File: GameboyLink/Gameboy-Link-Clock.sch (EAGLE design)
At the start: 37 parts, among them IC1 MEGA8-AI, J1 AVR_SPI_PRG_6PTH, Q1 16MHz, U1 DS1307Z, Y1 32.768kHz

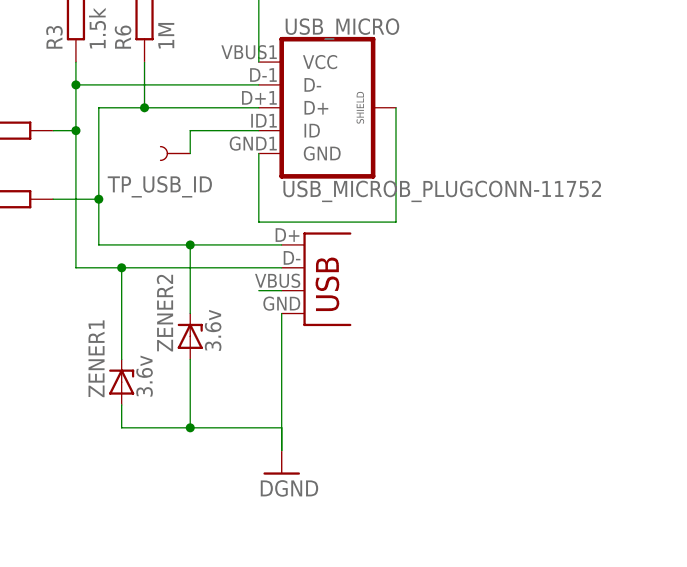
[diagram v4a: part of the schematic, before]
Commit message: Powers line done. Just noticed I forgot to wire ... THE GB LINK PORT to the MCU!!
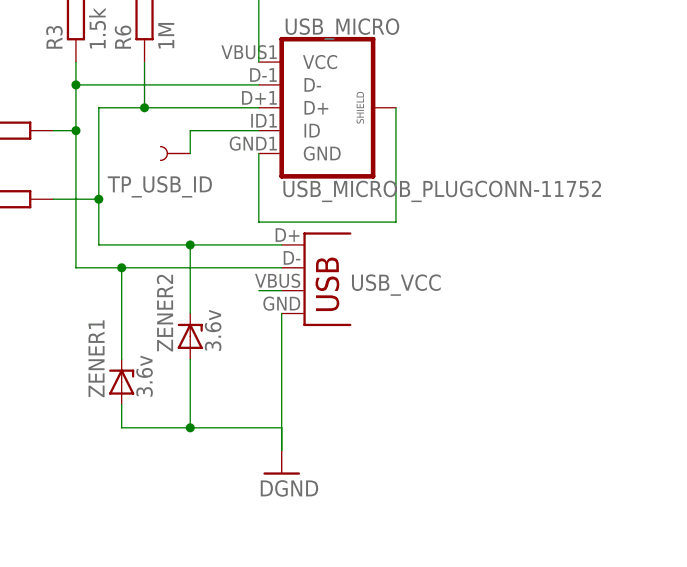
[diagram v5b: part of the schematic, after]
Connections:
- net USB_VCC: now also USB_MINI.VBUS
- net VCC: no longer USB_MINI.VBUS
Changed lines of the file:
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@@
-</segment>
-<segment>
-<pinref part="USB_MINI" gate="G$1" pin="VBUS"/>
-<wire x1="350.52" y1="-68.58" x2="353.06" y2="-68.58" width="0.1524" layer="91"/>
 </segment>
 <segment>
@@
 <label x="124.46" y="-45.72" size="1.778" layer="95"/>
 </segment>
-</net>
+<segment>
+<pinref part="USB_MINI" gate="G$1" pin="VBUS"/>
+<wire x1="350.52" y1="-68.58" x2="353.06" y2="-68.58" width="0.1524" layer="91"/>
+<label x="360.68" y="-68.58" size="1.778" layer="95"/>
+</segment>
+</net>

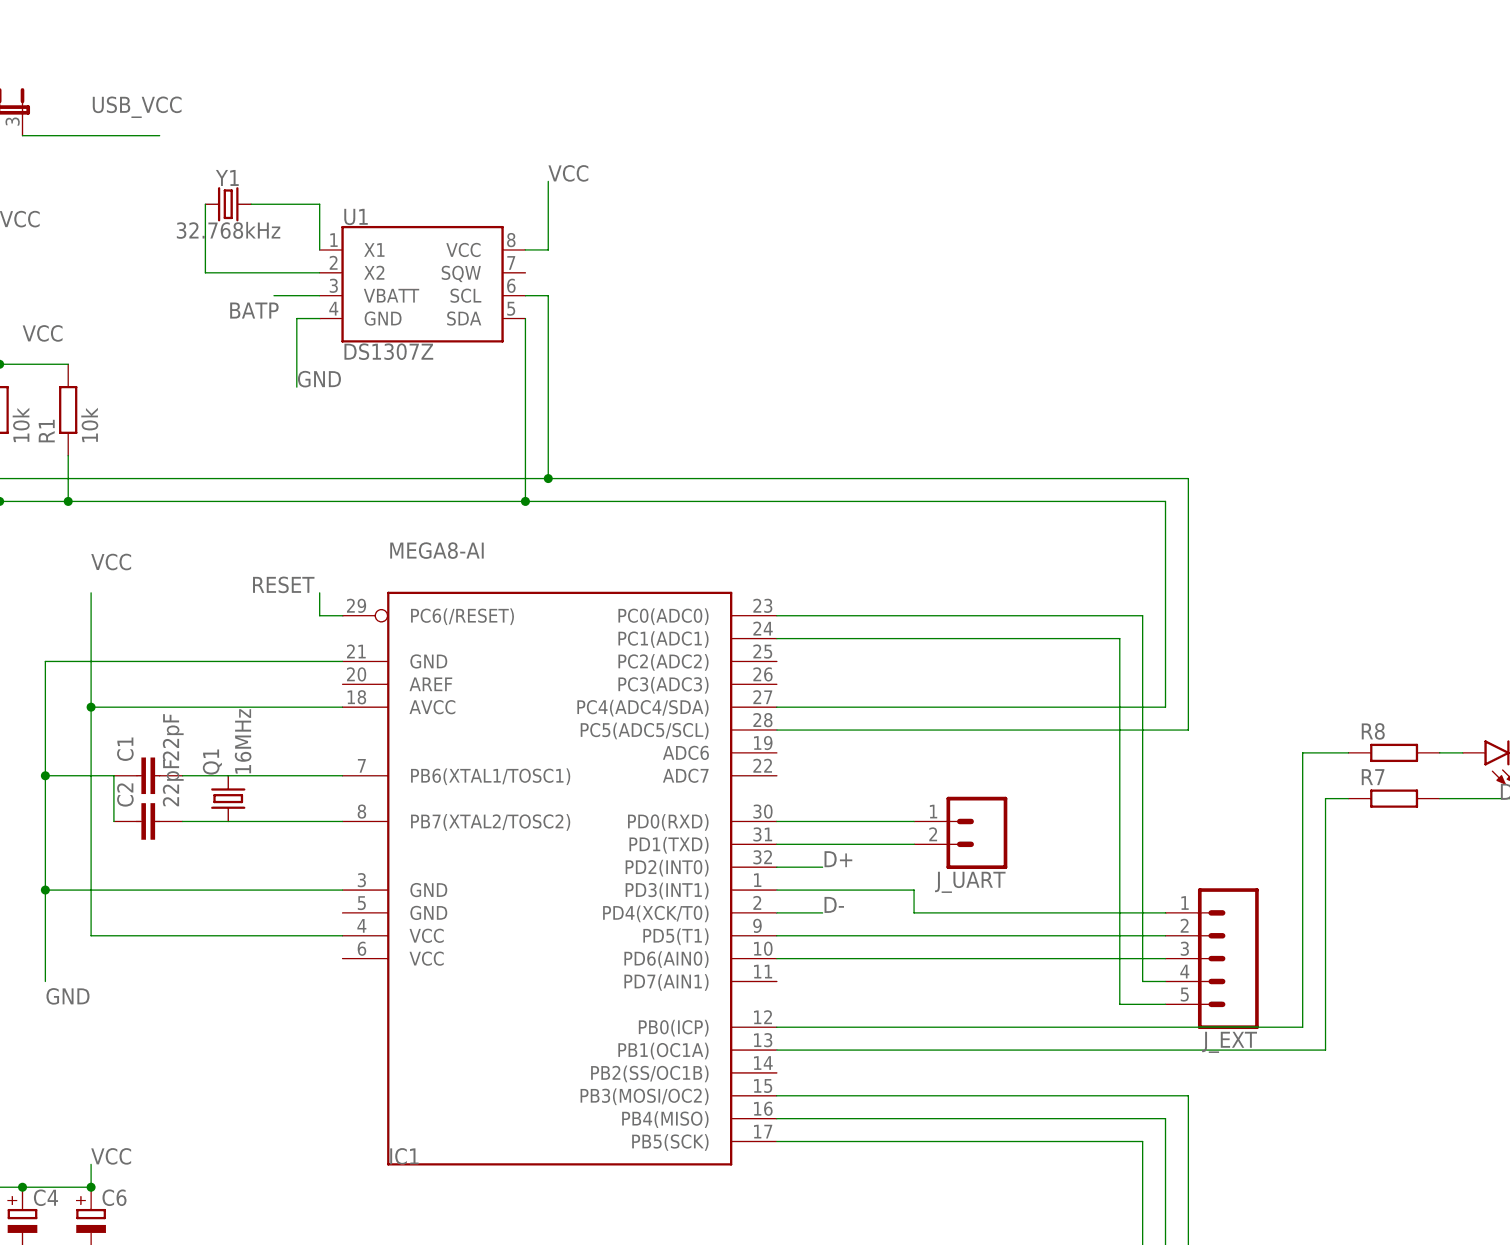
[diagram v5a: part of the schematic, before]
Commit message: All routed minus USB and ISP
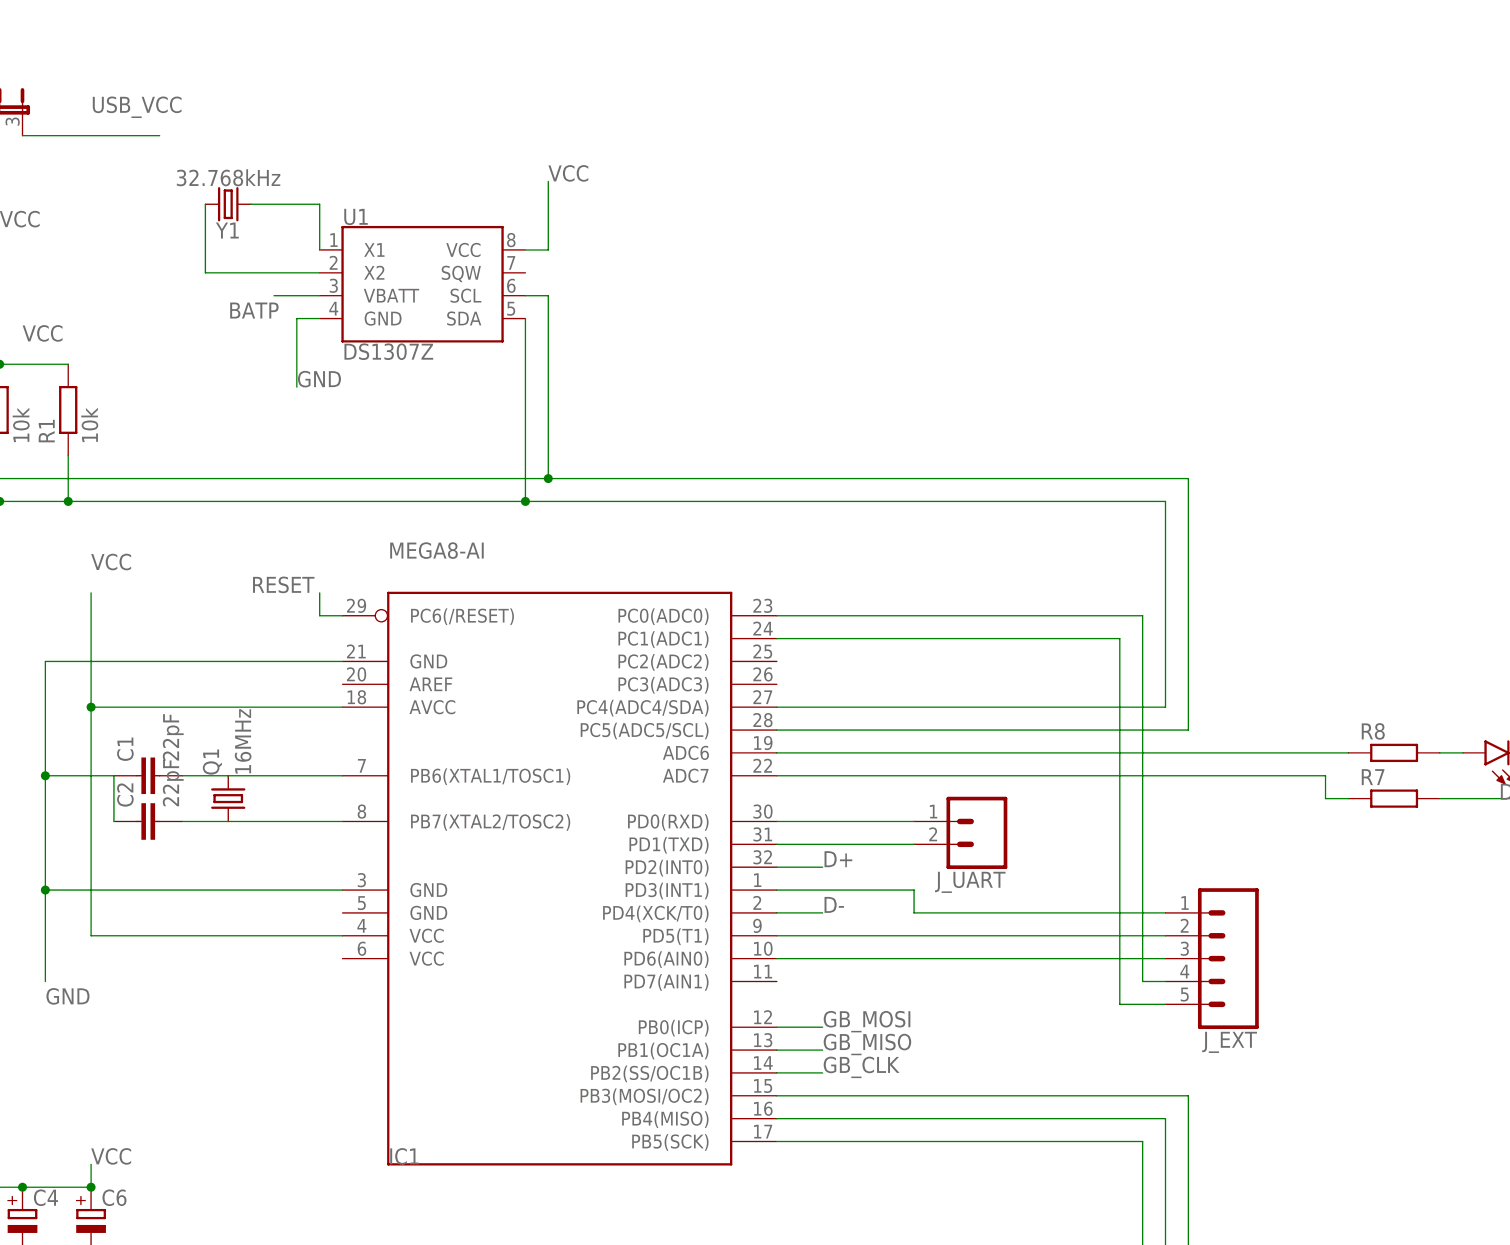
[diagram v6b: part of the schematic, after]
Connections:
- net GB_CLK: now also IC1.PB2(SS/OC1B)
- net GB_MISO: now also IC1.PB1(OC1A)
- net GB_MOSI: now also IC1.PB0(ICP)
- net N$21: now also IC1.ADC6; no longer IC1.PB0(ICP)
- net N$22: now also IC1.ADC7; no longer IC1.PB1(OC1A)
- net N$23: now also Y1.1; no longer Y1.2
- net N$24: now also Y1.2; no longer Y1.1
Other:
- moved on the sheet: Y1
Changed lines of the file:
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@@
 <setting verticaltext="up"/>
 </settings>
-<grid distance="0.1" unitdist="inch" unit="inch" style="lines" multiple="1" display="no" altdistance="0.01" altunitdist="inch" altunit="inch"/>
+<grid distance="0.1" unitdist="inch" unit="inch" style="lines" multiple="1" display="yes" altdistance="0.01" altunitdist="inch" altunit="inch"/>
 <layers>
 <layer number="1" name="Top" color="4" fill="1" visible="no" active="no"/>
@@
 <attribute name="VALUE" x="152.4" y="-71.374" size="1.778" layer="95" font="vector" align="top-left"/>
 </instance>
-<instance part="Y1" gate="G$1" x="139.7" y="-55.88" smashed="yes">
-<attribute name="NAME" x="139.7" y="-53.848" size="1.778" layer="95" font="vector" align="bottom-center"/>
-<attribute name="VALUE" x="139.7" y="-57.912" size="1.778" layer="96" font="vector" align="top-center"/>
+<instance part="Y1" gate="G$1" x="139.7" y="-55.88" smashed="yes" rot="R180">
+<attribute name="NAME" x="139.7" y="-57.912" size="1.778" layer="95" font="vector" rot="R180" align="bottom-center"/>
+<attribute name="VALUE" x="139.7" y="-53.848" size="1.778" layer="96" font="vector" rot="R180" align="top-center"/>
 </instance>
 <instance part="GBAC" gate="G$1" x="20.32" y="-45.72" smashed="yes" rot="R180">
@@
 <junction x="66.04" y="-40.64"/>
 </segment>
+<segment>
+<pinref part="IC1" gate="G$1" pin="PB2(SS/OC1B)"/>
+<wire x1="200.66" y1="-152.4" x2="205.74" y2="-152.4" width="0.1524" layer="91"/>
+<label x="205.74" y="-152.4" size="1.778" layer="95"/>
+</segment>
 </net>
 <net name="GB_SD" class="0">
@@
 <wire x1="68.58" y1="-63.5" x2="68.58" y2="-45.72" width="0.1524" layer="91"/>
 <junction x="68.58" y="-45.72"/>
+</segment>
+<segment>
+<pinref part="IC1" gate="G$1" pin="PB1(OC1A)"/>
+<wire x1="200.66" y1="-149.86" x2="205.74" y2="-149.86" width="0.1524" layer="91"/>
+<label x="205.74" y="-149.86" size="1.778" layer="95"/>
 </segment>
 </net>
@@
 <junction x="78.74" y="-48.26"/>
 </segment>
+<segment>
+<pinref part="IC1" gate="G$1" pin="PB0(ICP)"/>
+<wire x1="200.66" y1="-147.32" x2="205.74" y2="-147.32" width="0.1524" layer="91"/>
+<label x="205.74" y="-147.32" size="1.778" layer="95"/>
+</segment>
 </net>
 <net name="N$10" class="0">
@@
 <net name="N$21" class="0">
 <segment>
-<pinref part="IC1" gate="G$1" pin="PB0(ICP)"/>
-<wire x1="200.66" y1="-147.32" x2="259.08" y2="-147.32" width="0.1524" layer="91"/>
-<wire x1="259.08" y1="-147.32" x2="259.08" y2="-116.84" width="0.1524" layer="91"/>
 <pinref part="R8" gate="G$1" pin="1"/>
-<wire x1="259.08" y1="-116.84" x2="264.16" y2="-116.84" width="0.1524" layer="91"/>
+<pinref part="IC1" gate="G$1" pin="ADC6"/>
+<wire x1="264.16" y1="-116.84" x2="200.66" y2="-116.84" width="0.1524" layer="91"/>
 </segment>
 </net>
 <net name="N$22" class="0">
 <segment>
-<pinref part="IC1" gate="G$1" pin="PB1(OC1A)"/>
-<wire x1="200.66" y1="-149.86" x2="261.62" y2="-149.86" width="0.1524" layer="91"/>
-<wire x1="261.62" y1="-149.86" x2="261.62" y2="-121.92" width="0.1524" layer="91"/>
 <pinref part="R7" gate="G$1" pin="1"/>
 <wire x1="261.62" y1="-121.92" x2="264.16" y2="-121.92" width="0.1524" layer="91"/>
+<wire x1="261.62" y1="-121.92" x2="261.62" y2="-119.38" width="0.1524" layer="91"/>
+<pinref part="IC1" gate="G$1" pin="ADC7"/>
+<wire x1="261.62" y1="-119.38" x2="200.66" y2="-119.38" width="0.1524" layer="91"/>
 </segment>
 </net>
 <net name="N$23" class="0">
 <segment>
-<pinref part="Y1" gate="G$1" pin="2"/>
-<wire x1="142.24" y1="-55.88" x2="149.86" y2="-55.88" width="0.1524" layer="91"/>
 <pinref part="U1" gate="G$1" pin="X1"/>
 <wire x1="149.86" y1="-55.88" x2="149.86" y2="-60.96" width="0.1524" layer="91"/>
+<pinref part="Y1" gate="G$1" pin="1"/>
+<wire x1="142.24" y1="-55.88" x2="149.86" y2="-55.88" width="0.1524" layer="91"/>
 </segment>
 </net>
 <net name="N$24" class="0">
 <segment>
-<pinref part="Y1" gate="G$1" pin="1"/>
-<wire x1="137.16" y1="-55.88" x2="137.16" y2="-63.5" width="0.1524" layer="91"/>
 <pinref part="U1" gate="G$1" pin="X2"/>
 <wire x1="137.16" y1="-63.5" x2="149.86" y2="-63.5" width="0.1524" layer="91"/>
-</segment>
-</net>
+<pinref part="Y1" gate="G$1" pin="2"/>
+<wire x1="137.16" y1="-55.88" x2="137.16" y2="-63.5" width="0.1524" layer="91"/>
+</segment>
+</net>
